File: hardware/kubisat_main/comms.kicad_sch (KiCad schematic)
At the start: 1 part, among them U6 XL1278-SMT

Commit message: added microsd footprint
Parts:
- removed U6: XL1278-SMT, RF:XL1278-SMT, symbol RF:XL1278-SMT
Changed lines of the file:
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@@
 	(generator_version "8.0")
 	(paper "A4")
-	(symbol
-		(lib_id "RF:XL1278-SMT")
-		(at 165.1 87.63 0)
-		(unit 1)
-		(exclude_from_sim no)
-		(in_bom yes)
-		(on_board yes)
-		(dnp no)
-		(fields_autoplaced yes)
-		(property "Reference" "U6"
-			(at 165.1 58.42 0)
-			(effects
-				(font
-					(size 1.27 1.27)
-				)
-			)
-		)
-		(property "Value" "XL1278-SMT"
-			(at 165.1 60.96 0)
-			(effects
-				(font
-					(size 1.27 1.27)
-				)
-			)
-		)
-		(property "Footprint" "RF:XL1278-SMT"
-			(at 165.1 87.63 0)
-			(effects
-				(font
-					(size 1.27 1.27)
-				)
-				(hide yes)
-			)
-		)
-		(property "Datasheet" ""
-			(at 165.1 87.63 0)
-			(effects
-				(font
-					(size 1.27 1.27)
-				)
-				(hide yes)
-			)
-		)
-		(property "Description" ""
-			(at 165.1 87.63 0)
-			(effects
-				(font
-					(size 1.27 1.27)
-				)
-				(hide yes)
-			)
-		)
-		(pin "15"
-		)
-		(pin "6"
-		)
-		(pin "14"
-		)
-		(pin "4"
-		)
-		(pin "7"
-		)
-		(pin "8"
-		)
-		(pin "5"
-		)
-		(pin "12"
-		)
-		(pin "3"
-		)
-		(pin "16"
-		)
-		(pin "9"
-		)
-		(pin "13"
-		)
-		(pin "10"
-		)
-		(pin "1"
-		)
-		(pin "11"
-		)
-		(pin "2"
-		)
-		(instances
-			(project ""
-				(path "/8e012760-7134-459b-b212-1cb69dd2e1ec/2c86e300-786b-4193-97e9-c91ab29cb54d"
-					(reference "U6")
-					(unit 1)
-				)
-			)
-		)
-	)
 )

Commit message: added arduino code, more items on main schematic
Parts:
- added U6: SX1278, Package_DFN_QFN:QFN-28-1EP_6x6mm_P0.65mm_EP4.8x4.8mm, symbol RF:SX1278
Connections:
- new net: U6.15 (GND), U6.21 (GND), U6.22 (GND), U6.23 (GND), U6.26 (GND), U6.29 (GND)
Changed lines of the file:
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@@
 	(generator_version "8.0")
 	(paper "A4")
+	(symbol
+		(lib_id "RF:SX1278")
+		(at 73.66 64.77 0)
+		(unit 1)
+		(exclude_from_sim no)
+		(in_bom yes)
+		(on_board yes)
+		(dnp no)
+		(fields_autoplaced yes)
+		(property "Reference" "U6"
+			(at 75.8541 92.71 0)
+			(effects
+				(font
+					(size 1.27 1.27)
+				)
+				(justify left)
+			)
+		)
+		(property "Value" "SX1278"
+			(at 75.8541 95.25 0)
+			(effects
+				(font
+					(size 1.27 1.27)
+				)
+				(justify left)
+			)
+		)
+		(property "Footprint" "Package_DFN_QFN:QFN-28-1EP_6x6mm_P0.65mm_EP4.8x4.8mm"
+			(at 73.66 72.39 0)
+			(effects
+				(font
+					(size 1.27 1.27)
+				)
+				(hide yes)
+			)
+		)
+		(property "Datasheet" "https://semtech.my.salesforce.com/sfc/p/#E0000000JelG/a/2R0000001Rbr/6EfVZUorrpoKFfvaF_Fkpgp5kzjiNyiAbqcpqh9qSjE"
+			(at 73.66 69.85 0)
+			(effects
+				(font
+					(size 1.27 1.27)
+				)
+				(hide yes)
+			)
+		)
+		(property "Description" "137 MHz to 525 MHz Low Power Long Range Transceiver, spreading factor from 6 to 12, LoRA, QFN-28"
+			(at 73.66 64.77 0)
+			(effects
+				(font
+					(size 1.27 1.27)
+				)
+				(hide yes)
+			)
+		)
+		(pin "16"
+		)
+		(pin "6"
+		)
+		(pin "3"
+		)
+		(pin "29"
+		)
+		(pin "17"
+		)
+		(pin "1"
+		)
+		(pin "18"
+		)
+		(pin "2"
+		)
+		(pin "19"
+		)
+		(pin "22"
+		)
+		(pin "10"
+		)
+		(pin "11"
+		)
+		(pin "23"
+		)
+		(pin "27"
+		)
+		(pin "21"
+		)
+		(pin "15"
+		)
+		(pin "9"
+		)
+		(pin "7"
+		)
+		(pin "8"
+		)
+		(pin "25"
+		)
+		(pin "28"
+		)
+		(pin "12"
+		)
+		(pin "24"
+		)
+		(pin "4"
+		)
+		(pin "14"
+		)
+		(pin "5"
+		)
+		(pin "20"
+		)
+		(pin "26"
+		)
+		(pin "13"
+		)
+		(instances
+			(project ""
+				(path "/8e012760-7134-459b-b212-1cb69dd2e1ec/2c86e300-786b-4193-97e9-c91ab29cb54d"
+					(reference "U6")
+					(unit 1)
+				)
+			)
+		)
+	)
 )

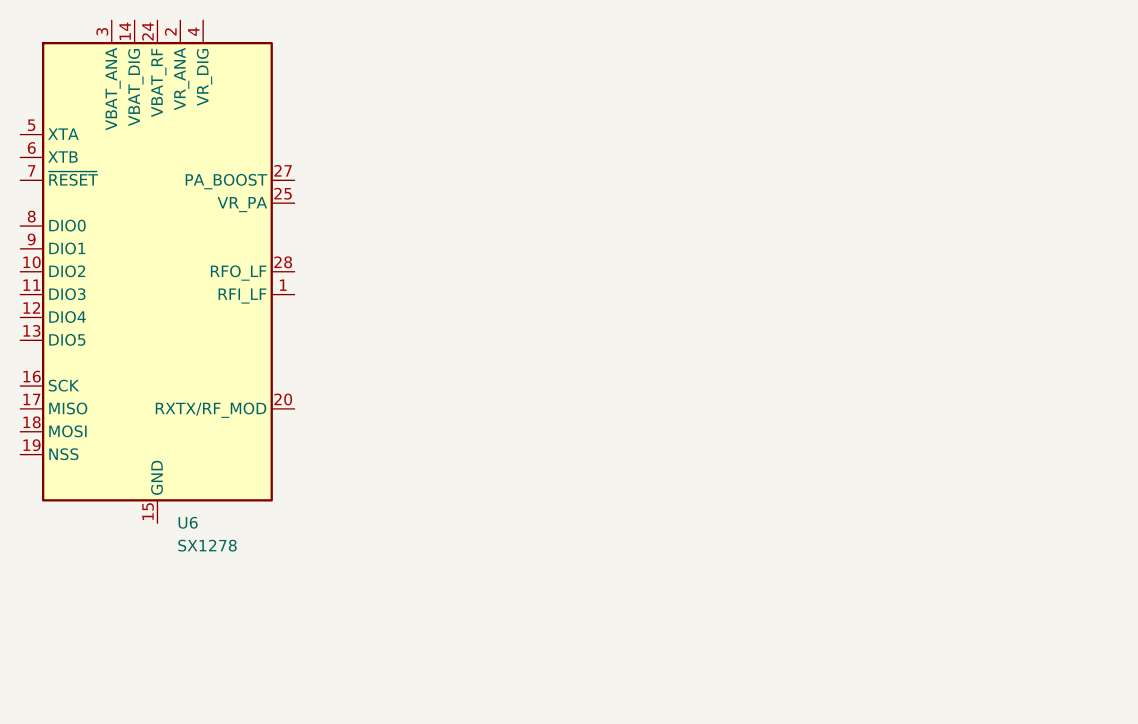
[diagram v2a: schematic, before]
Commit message: added elements and traces to main pcb
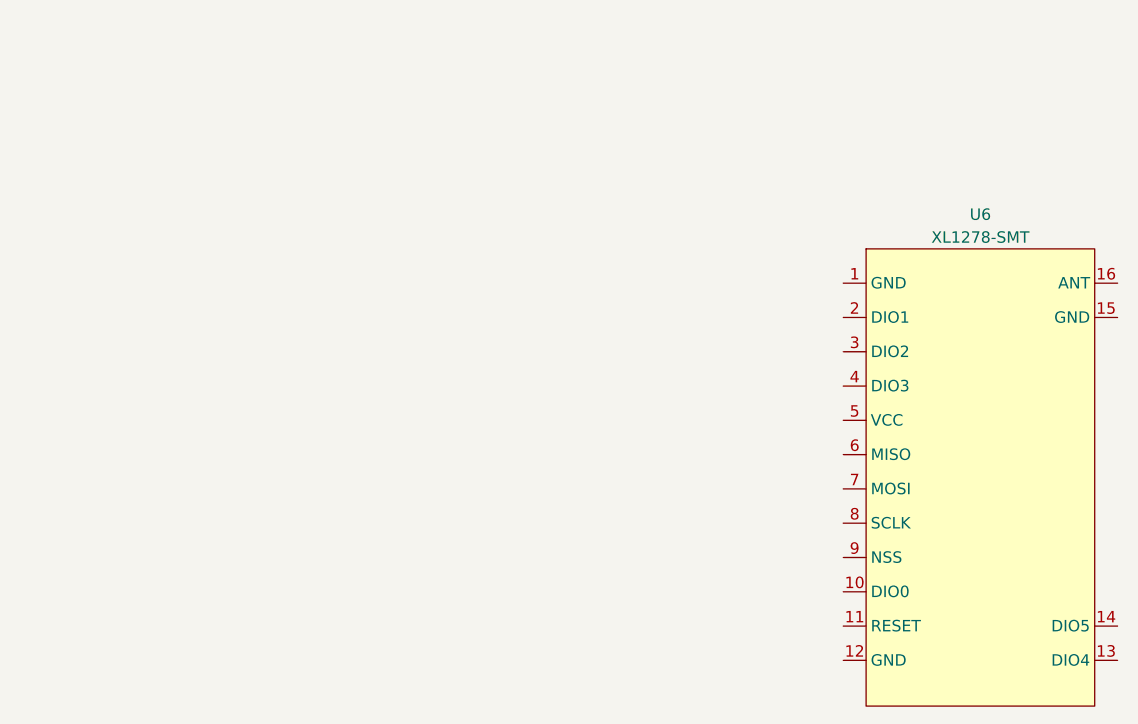
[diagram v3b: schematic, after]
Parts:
- removed U6: SX1278, Package_DFN_QFN:QFN-28-1EP_6x6mm_P0.65mm_EP4.8x4.8mm, symbol RF:SX1278
- added U6: XL1278-SMT, RF:XL1278-SMT, symbol RF:XL1278-SMT
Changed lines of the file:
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@@
 	(paper "A4")
 	(symbol
-		(lib_id "RF:SX1278")
-		(at 73.66 64.77 0)
+		(lib_id "RF:XL1278-SMT")
+		(at 165.1 87.63 0)
 		(unit 1)
 		(exclude_from_sim no)
@@
 		(fields_autoplaced yes)
 		(property "Reference" "U6"
-			(at 75.8541 92.71 0)
+			(at 165.1 58.42 0)
 			(effects
 				(font
 					(size 1.27 1.27)
 				)
-				(justify left)
 			)
 		)
-		(property "Value" "SX1278"
-			(at 75.8541 95.25 0)
+		(property "Value" "XL1278-SMT"
+			(at 165.1 60.96 0)
 			(effects
 				(font
 					(size 1.27 1.27)
 				)
-				(justify left)
 			)
 		)
-		(property "Footprint" "Package_DFN_QFN:QFN-28-1EP_6x6mm_P0.65mm_EP4.8x4.8mm"
-			(at 73.66 72.39 0)
+		(property "Footprint" "RF:XL1278-SMT"
+			(at 165.1 87.63 0)
 			(effects
 				(font
@@
 			)
 		)
-		(property "Datasheet" "https://semtech.my.salesforce.com/sfc/p/#E0000000JelG/a/2R0000001Rbr/6EfVZUorrpoKFfvaF_Fkpgp5kzjiNyiAbqcpqh9qSjE"
-			(at 73.66 69.85 0)
+		(property "Datasheet" ""
+			(at 165.1 87.63 0)
 			(effects
 				(font
@@
 			)
 		)
-		(property "Description" "137 MHz to 525 MHz Low Power Long Range Transceiver, spreading factor from 6 to 12, LoRA, QFN-28"
-			(at 73.66 64.77 0)
+		(property "Description" ""
+			(at 165.1 87.63 0)
 			(effects
 				(font
@@
 			)
 		)
-		(pin "16"
+		(pin "15"
 		)
 		(pin "6"
 		)
-		(pin "3"
+		(pin "14"
 		)
-		(pin "29"
-		)
-		(pin "17"
-		)
-		(pin "1"
-		)
-		(pin "18"
-		)
-		(pin "2"
-		)
-		(pin "19"
-		)
-		(pin "22"
-		)
-		(pin "10"
-		)
-		(pin "11"
-		)
-		(pin "23"
-		)
-		(pin "27"
-		)
-		(pin "21"
-		)
-		(pin "15"
-		)
-		(pin "9"
+		(pin "4"
 		)
 		(pin "7"
@@
 		(pin "8"
 		)
-		(pin "25"
-		)
-		(pin "28"
+		(pin "5"
 		)
 		(pin "12"
 		)
-		(pin "24"
+		(pin "3"
 		)
-		(pin "4"
+		(pin "16"
 		)
-		(pin "14"
-		)
-		(pin "5"
-		)
-		(pin "20"
-		)
-		(pin "26"
+		(pin "9"
 		)
 		(pin "13"
 		)
+		(pin "10"
+		)
+		(pin "1"
+		)
+		(pin "11"
+		)
+		(pin "2"
+		)
 		(instances
